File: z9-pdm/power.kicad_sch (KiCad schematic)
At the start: 28 parts, among them U1 B0505XT-1WR3, U22 TLV76733DRVx, U6 LMR14206

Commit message: mainly route vip
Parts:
- removed C27, C28: 10uF, PCM_JLCPCB:C_0603, symbol PCM_JLCPCB-Capacitors:0603,10uF,(2)
- removed U1: B0505XT-1WR3, dnt:B0505_Isolated_SMD, symbol dnt_global:B0505_Isolated_SMD

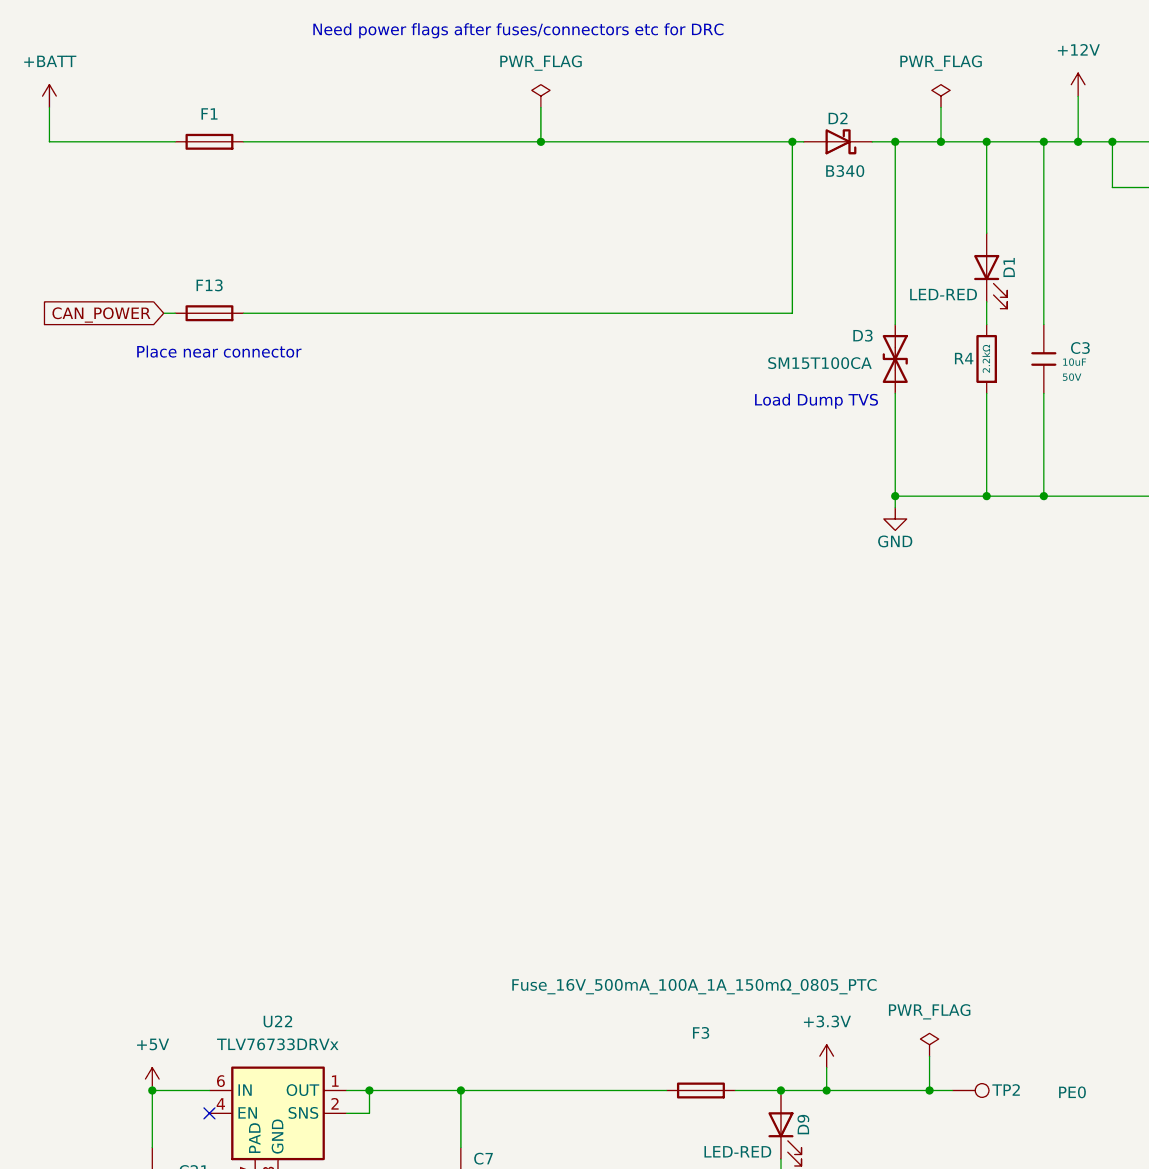
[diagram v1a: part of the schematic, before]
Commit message: rearrange power section for inductive load and fix fusing (none) wire uyp second vipower
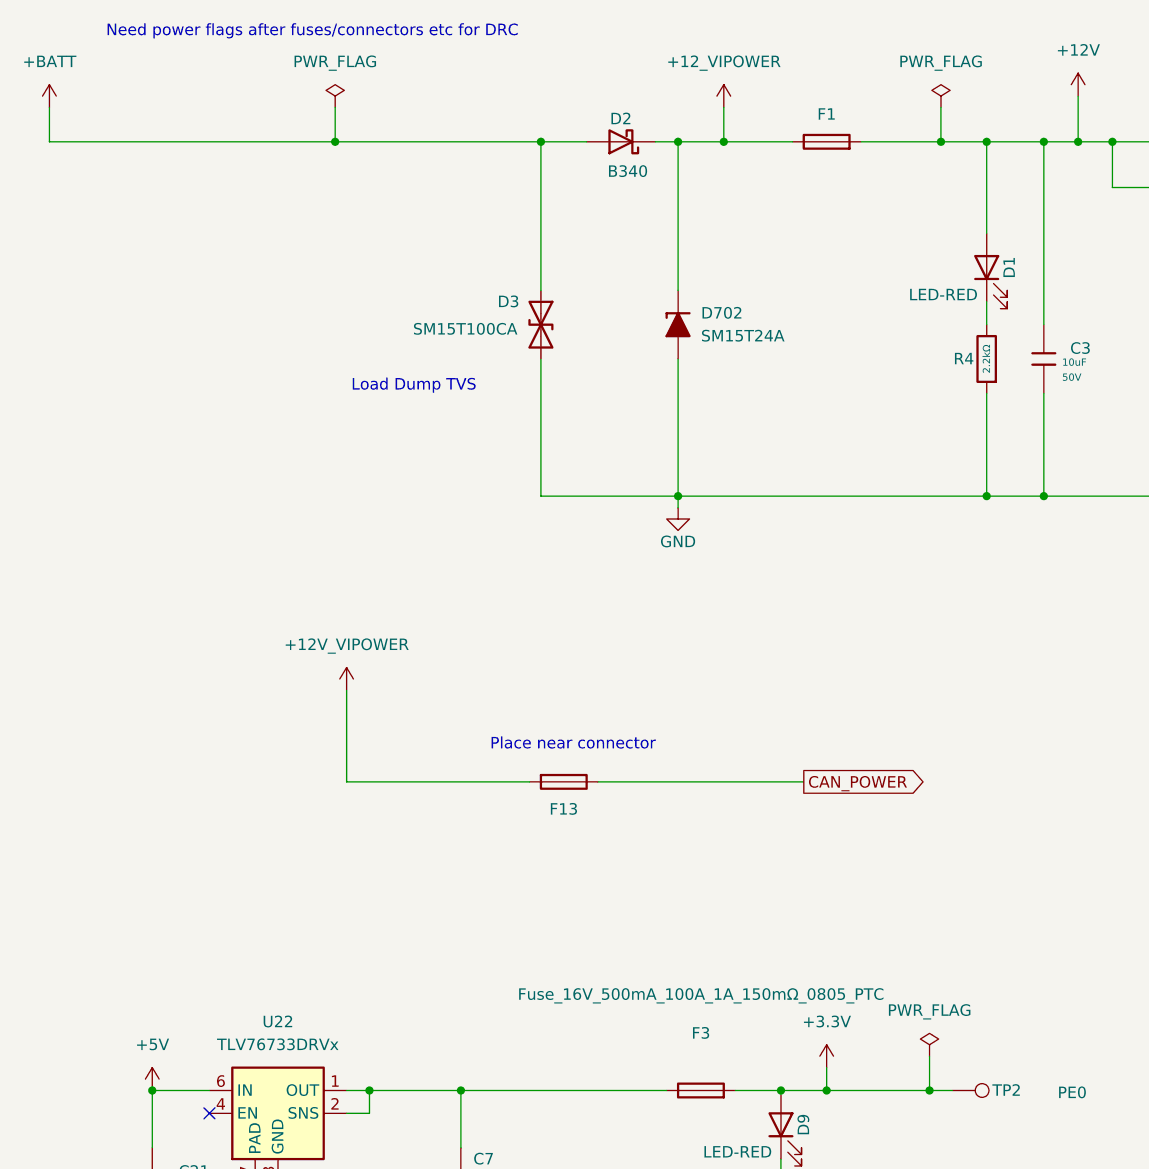
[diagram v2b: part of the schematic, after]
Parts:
- added D702: SM15T24A, PCM_Diode_SMD_AKL:D_SMC, symbol dnt_global:SM15T24A
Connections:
- net +12V: now also F1.2; no longer D2.1 (K), D3.1 (A1)
- net +BATT: now also D2.2 (A), D3.1 (A1); no longer F1.1
- net GND: now also D702.2 (A)
- new net +12V_VIPOWER: F13.2
- new net +12_VIPOWER: D2.1 (K), D702.1 (K), F1.1
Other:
- moved on the sheet: D2, D3, F1, F13

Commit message: vipower fixes etc
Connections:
- net +12_VIPOWER is gone; now on net +12V_VIPOWER: D2.1 (K), D702.1 (K), F1.1
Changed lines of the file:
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@@
 			)
 		)
-		(property "Value" "+12_VIPOWER"
+		(property "Value" "+12V_VIPOWER"
 			(at 92.71 25.4 0)
 			(effects
